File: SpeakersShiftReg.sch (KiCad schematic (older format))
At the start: 26 parts, among them J1 CONN, J10 Conn_01x08_Male, J11 Conn_01x08_Male, J12 Conn_01x08_Male, J13 Conn_01x08_Male, J2 CONN, J3 CONN, J4 CONN, J5 CONN, J6 CONN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

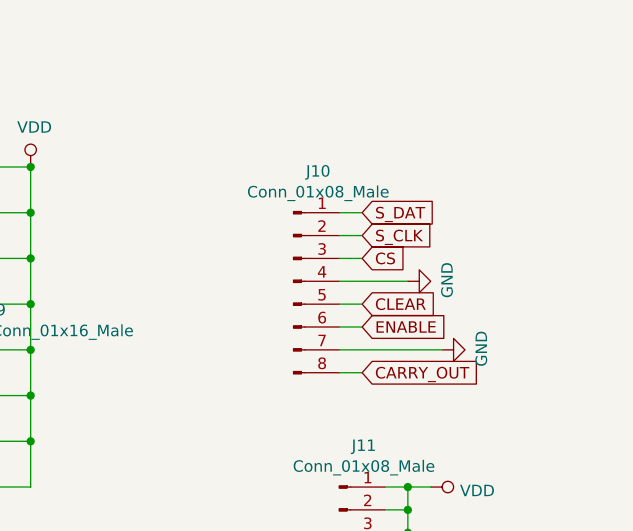
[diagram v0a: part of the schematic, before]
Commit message: added silk, ready for traces
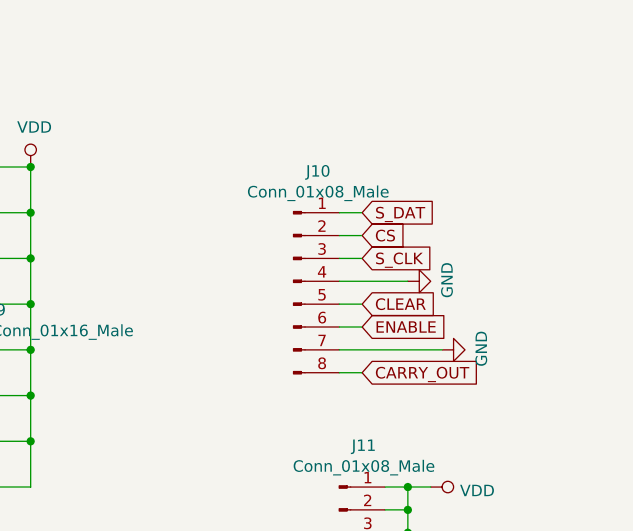
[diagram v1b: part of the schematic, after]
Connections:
- net CS: now also J10.2 (Pin_2); no longer J10.3 (Pin_3)
- net S_CLK: now also J10.3 (Pin_3); no longer J10.2 (Pin_2)
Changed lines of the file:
@@
 Text GLabel 8150 1900 2    50   Input ~ 0
 S_DAT
+Text GLabel 8150 2100 2    50   Input ~ 0
+S_CLK
 Text GLabel 8150 2000 2    50   Input ~ 0
-S_CLK
-Text GLabel 8150 2100 2    50   Input ~ 0
 CS
 Text GLabel 8150 2300 2    50   Input ~ 0

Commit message: commit before trying thing
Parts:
- added C1: 0.1uf, Capacitor_THT:C_Disc_D3.0mm_W2.0mm_P2.50mm, symbol Device:C
- added C2: 10uf, Capacitor_THT:CP_Radial_D5.0mm_P2.00mm, symbol Device:CP
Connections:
- net +5V: now also C1.1, C2.1
- net GND: now also C1.2, C2.2
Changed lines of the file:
@@
 Connection ~ 8950 5500
 Wire Wire Line
-	8950 5500 8950 5400
+	8950 5500 8950 5450
 Wire Wire Line
 	8800 5700 9150 5700
 Wire Wire Line
-	9150 5700 9150 5800
+	9150 5700 9150 5750
 Wire Wire Line
 	8800 5800 9150 5800
@@
 Wire Wire Line
 	8950 5900 9150 5900
+$Comp
+L Device:C C1
+U 1 1 5EE9D0A9
+P 9300 5600
+F 0 "C1" H 9415 5646 50  0000 L CNN
+F 1 "0.1uf" H 9415 5555 50  0000 L CNN
+F 2 "Capacitor_THT:C_Disc_D3.0mm_W2.0mm_P2.50mm" H 9338 5450 50  0001 C CNN
+F 3 "~" H 9300 5600 50  0001 C CNN
+	1    9300 5600
+	1    0    0    -1
+$EndComp
+Wire Wire Line
+	8950 5450 9200 5450
+Connection ~ 8950 5450
+Wire Wire Line
+	8950 5450 8950 5400
+Wire Wire Line
+	9150 5750 9200 5750
+Connection ~ 9150 5750
+Wire Wire Line
+	9150 5750 9150 5800
+$Comp
+L Device:CP C2
+U 1 1 5EEAD2D3
+P 9750 5600
+F 0 "C2" H 9868 5646 50  0000 L CNN
+F 1 "10uf" H 9868 5555 50  0000 L CNN
+F 2 "Capacitor_THT:CP_Radial_D5.0mm_P2.00mm" H 9788 5450 50  0001 C CNN
+F 3 "~" H 9750 5600 50  0001 C CNN
+	1    9750 5600
+	1    0    0    -1
+$EndComp
+Wire Wire Line
+	9200 5450 9200 5350
+Wire Wire Line
+	9200 5350 9750 5350
+Wire Wire Line
+	9750 5350 9750 5450
+Connection ~ 9200 5450
+Wire Wire Line
+	9200 5450 9300 5450
+Wire Wire Line
+	9200 5750 9200 5800
+Wire Wire Line
+	9200 5800 9750 5800
+Wire Wire Line
+	9750 5800 9750 5750
+Connection ~ 9200 5750
+Wire Wire Line
+	9200 5750 9300 5750
 $EndSCHEMATC

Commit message: finish layout
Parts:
- added C3, C4: 10uf, Capacitor_THT:CP_Radial_D5.0mm_P2.00mm, symbol Device:CP
- J10, J11, J12, J13: symbol Connector:Conn_01x08_Male -> Connector:Conn_01x06_Male
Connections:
- net +5V: now also J13.4 (Pin_4); no longer J13.7 (Pin_7), J13.8 (Pin_8)
- net CARRY_OUT: now also J10.6 (Pin_6); no longer J10.8 (Pin_8)
- net CLEAR: now also J10.4 (Pin_4); no longer J10.5 (Pin_5)
- net ENABLE: now also J10.5 (Pin_5); no longer J10.6 (Pin_6)
- net GND: now also C3.2, C4.2; no longer J10.4 (Pin_4), J10.7 (Pin_7), J12.7 (Pin_7), J12.8 (Pin_8), J13.4 (Pin_4)
- net VDD: now also C3.1, C4.1; no longer J11.7 (Pin_7), J11.8 (Pin_8)
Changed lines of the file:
@@
 	6200 3000 6300 3000
 $Comp
-L Connector:Conn_01x08_Male J10
+L Connector:Conn_01x06_Male J10
 U 1 1 5ED7FDFD
-P 7850 2200
-F 0 "J10" H 7958 2681 50  0000 C CNN
-F 1 "Conn_01x08_Male" H 7958 2590 50  0000 C CNN
-F 2 "Connector_PinSocket_2.54mm:PinSocket_1x08_P2.54mm_Vertical" H 7850 2200 50  0001 C CNN
-F 3 "~" H 7850 2200 50  0001 C CNN
-	1    7850 2200
+P 7850 2100
+F 0 "J10" H 7958 2481 50  0000 C CNN
+F 1 "Conn_01x08_Male" H 7958 2390 50  0000 C CNN
+F 2 "Connector_PinSocket_2.54mm:PinSocket_1x08_P2.54mm_Vertical" H 7850 2100 50  0001 C CNN
+F 3 "~" H 7850 2100 50  0001 C CNN
+	1    7850 2100
 	1    0    0    -1
 $EndComp
@@
 Text GLabel 8150 2000 2    50   Input ~ 0
 CS
+Text GLabel 8150 2200 2    50   Input ~ 0
+CLEAR
 Text GLabel 8150 2300 2    50   Input ~ 0
-CLEAR
-Text GLabel 8150 2400 2    50   Input ~ 0
 ENABLE
-Text GLabel 8150 2600 2    50   Input ~ 0
-CARRY_OUT
-$Comp
-L power:GND #PWR0102
-U 1 1 5ED82C84
-P 8350 2200
-F 0 "#PWR0102" H 8350 1950 50  0001 C CNN
-F 1 "GND" H 8355 2027 50  0000 C CNN
-F 2 "" H 8350 2200 50  0001 C CNN
-F 3 "" H 8350 2200 50  0001 C CNN
-	1    8350 2200
-	0    -1   -1   0
-$EndComp
-$Comp
-L power:GND #PWR0103
-U 1 1 5ED833B2
-P 8500 2500
-F 0 "#PWR0103" H 8500 2250 50  0001 C CNN
-F 1 "GND" H 8505 2327 50  0000 C CNN
-F 2 "" H 8500 2500 50  0001 C CNN
-F 3 "" H 8500 2500 50  0001 C CNN
-	1    8500 2500
-	0    -1   -1   0
-$EndComp
 Wire Wire Line
 	8050 1900 8150 1900
@@
 	8050 2100 8150 2100
 Wire Wire Line
-	8050 2200 8350 2200
+	8050 2200 8150 2200
 Wire Wire Line
 	8050 2300 8150 2300
-Wire Wire Line
-	8050 2400 8150 2400
-Wire Wire Line
-	8050 2600 8150 2600
-Wire Wire Line
-	8050 2500 8500 2500
-$Comp
-L Connector:Conn_01x08_Male J11
+$Comp
+L Connector:Conn_01x06_Male J11
 U 1 1 5EDB5AB8
-P 8050 3400
-F 0 "J11" H 8158 3881 50  0000 C CNN
-F 1 "Conn_01x08_Male" H 8158 3790 50  0000 C CNN
-F 2 "Connector_PinSocket_2.54mm:PinSocket_1x08_P2.54mm_Vertical" H 8050 3400 50  0001 C CNN
-F 3 "~" H 8050 3400 50  0001 C CNN
-	1    8050 3400
+P 8050 3300
+F 0 "J11" H 8158 3681 50  0000 C CNN
+F 1 "Conn_01x08_Male" H 8158 3590 50  0000 C CNN
+F 2 "Connector_PinSocket_2.54mm:PinSocket_1x08_P2.54mm_Vertical" H 8050 3300 50  0001 C CNN
+F 3 "~" H 8050 3300 50  0001 C CNN
+	1    8050 3300
 	1    0    0    -1
 $EndComp
@@
 Wire Wire Line
 	8350 3100 8350 3200
-Wire Wire Line
-	8350 3800 8250 3800
 Connection ~ 8350 3100
 Wire Wire Line
 	8350 3100 8450 3100
 Wire Wire Line
-	8250 3700 8350 3700
-Connection ~ 8350 3700
-Wire Wire Line
-	8350 3700 8350 3800
-Wire Wire Line
 	8250 3600 8350 3600
-Connection ~ 8350 3600
-Wire Wire Line
-	8350 3600 8350 3700
 Wire Wire Line
 	8250 3500 8350 3500
@@
 Connection ~ 8350 3200
 Wire Wire Line
-	8350 3200 8350 3300
-$Comp
-L Connector:Conn_01x08_Male J12
+	8350 3200 8350 3250
+$Comp
+L Connector:Conn_01x06_Male J12
 U 1 1 5EDDE8A4
-P 8300 4450
-F 0 "J12" H 8408 4931 50  0000 C CNN
-F 1 "Conn_01x08_Male" H 8408 4840 50  0000 C CNN
-F 2 "Connector_PinSocket_2.54mm:PinSocket_1x08_P2.54mm_Vertical" H 8300 4450 50  0001 C CNN
-F 3 "~" H 8300 4450 50  0001 C CNN
-	1    8300 4450
+P 8300 4350
+F 0 "J12" H 8408 4731 50  0000 C CNN
+F 1 "Conn_01x08_Male" H 8408 4640 50  0000 C CNN
+F 2 "Connector_PinSocket_2.54mm:PinSocket_1x08_P2.54mm_Vertical" H 8300 4350 50  0001 C CNN
+F 3 "~" H 8300 4350 50  0001 C CNN
+	1    8300 4350
 	1    0    0    -1
 $EndComp
@@
 Wire Wire Line
 	8600 4150 8600 4250
-Wire Wire Line
-	8600 4850 8500 4850
 Connection ~ 8600 4150
 Wire Wire Line
 	8600 4150 8700 4150
 Wire Wire Line
-	8500 4750 8600 4750
-Connection ~ 8600 4750
-Wire Wire Line
-	8600 4750 8600 4850
-Wire Wire Line
 	8500 4650 8600 4650
-Connection ~ 8600 4650
-Wire Wire Line
-	8600 4650 8600 4750
 Wire Wire Line
 	8500 4550 8600 4550
@@
 $EndComp
 $Comp
-L Connector:Conn_01x08_Male J13
+L Connector:Conn_01x06_Male J13
 U 1 1 5EDE6D3F
 P 8600 5700
@@
 $EndComp
 Wire Wire Line
-	8800 5300 8950 5300
-Wire Wire Line
-	8800 5600 8950 5600
-Wire Wire Line
-	8950 5600 8950 5500
-Connection ~ 8950 5300
-Wire Wire Line
 	8950 5300 9150 5300
 Wire Wire Line
@@
 Wire Wire Line
 	8800 5500 8950 5500
-Connection ~ 8950 5500
 Wire Wire Line
 	8950 5500 8950 5450
@@
 Wire Wire Line
 	9150 5800 9150 5900
-Wire Wire Line
-	8800 5900 8950 5900
 Connection ~ 9150 5900
 Wire Wire Line
 	9150 5900 9150 6000
-Wire Wire Line
-	8800 6000 8950 6000
-Wire Wire Line
-	8950 6000 8950 5900
-Connection ~ 8950 5900
-Wire Wire Line
-	8950 5900 9150 5900
 $Comp
 L Device:C C1
@@
 Wire Wire Line
 	9200 5750 9300 5750
+$Comp
+L Device:CP C3
+U 1 1 5EEDA483
+P 8700 3500
+F 0 "C3" H 8818 3546 50  0000 L CNN
+F 1 "10uf" H 8818 3455 50  0000 L CNN
+F 2 "Capacitor_THT:CP_Radial_D5.0mm_P2.00mm" H 8738 3350 50  0001 C CNN
+F 3 "~" H 8700 3500 50  0001 C CNN
+	1    8700 3500
+	1    0    0    -1
+$EndComp
+$Comp
+L Device:CP C4
+U 1 1 5EEDB0CE
+P 9150 3500
+F 0 "C4" H 9268 3546 50  0000 L CNN
+F 1 "10uf" H 9268 3455 50  0000 L CNN
+F 2 "Capacitor_THT:CP_Radial_D5.0mm_P2.00mm" H 9188 3350 50  0001 C CNN
+F 3 "~" H 9150 3500 50  0001 C CNN
+	1    9150 3500
+	1    0    0    -1
+$EndComp
+$Comp
+L power:GND #PWR0102
+U 1 1 5EEDB728
+P 9150 3750
+F 0 "#PWR0102" H 9150 3500 50  0001 C CNN
+F 1 "GND" H 9155 3577 50  0000 C CNN
+F 2 "" H 9150 3750 50  0001 C CNN
+F 3 "" H 9150 3750 50  0001 C CNN
+	1    9150 3750
+	1    0    0    -1
+$EndComp
+Wire Wire Line
+	8350 3250 8700 3250
+Wire Wire Line
+	9150 3250 9150 3350
+Connection ~ 8350 3250
+Wire Wire Line
+	8350 3250 8350 3300
+Wire Wire Line
+	8700 3350 8700 3250
+Connection ~ 8700 3250
+Wire Wire Line
+	8700 3250 9150 3250
+Wire Wire Line
+	9150 3650 9150 3700
+Wire Wire Line
+	8700 3650 8700 3700
+Wire Wire Line
+	8700 3700 9150 3700
+Connection ~ 9150 3700
+Wire Wire Line
+	9150 3700 9150 3750
+Wire Wire Line
+	8800 5600 8950 5600
+Wire Wire Line
+	8950 5600 8950 5500
+Connection ~ 8950 5500
+Wire Wire Line
+	8800 5900 9150 5900
+Wire Wire Line
+	8050 2400 8150 2400
+Text GLabel 8150 2400 2    50   Input ~ 0
+CARRY_OUT
 $EndSCHEMATC
